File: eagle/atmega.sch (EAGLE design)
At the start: 40 parts, among them IC1 TO 5V, Q1 16MHz, U1 ATMEGA328P-AU

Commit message: Ładniej wygląda, dodałem transobtor zamiast fotorezystorów. Podłączenie komparatorów
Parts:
- removed FOTO1, FOTO2, FOTO3, FOTO4: (no value), pinhead:PINHD-1X3
- removed PH1, PH2, PH3, PH4: M9960_11B, photo-elements:M9960_11B
- added IC2: LM339D, linear:LM339D
- added JP1, JP2, JP3, JP4: (no value), pinhead:PINHD-1X3
- added R10, R14, R17: 100k, rcl:R-EU_R0805
- added R11: 220, rcl:R-EU_R0805
- added R12, R15, R18, R7, R8: 220R, rcl:R-EU_R0805
- added R13, R16, R9: 22k, rcl:R-EU_R0805
- added U$2, U$3, U$4, U$5: CNY70, cny70:CNY70
- LED1, LED3, LED4, LED5: device led:LED5MM -> led:LEDCHIPLED_0805
- R1: device resistor:R-EU_0204/7 -> rcl:R-EU_R0805
- R2: value (none) -> 220R; device resistor:R-EU_M0805 -> rcl:R-EU_R0805
- R3: value (none) -> 22k; device resistor:R-EU_0204/5 -> rcl:R-EU_R0805
- R4: value (none) -> 100k; device resistor:R-EU_0204/5 -> rcl:R-EU_R0805
- R5, R6: value (none) -> 220R; device resistor:R-EU_0204/5 -> rcl:R-EU_R0805
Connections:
- net N$2 renamed KWARC1
- net N$3 renamed KWARC2
- removed net N$33: FOTO4.3, U1.PC3
- removed net PC0: PH1.2, R3.1
- removed net PC1: PH2.2, R4.1
- removed net PC2: PH3.2, R5.1
- removed net PC3: PH4.2, R6.1
- new net KO1: IC2A.OUT, PROGRAMMER.1, R4.1, R6.1, U1.PB5
- new net KO2: IC2B.OUT, PROGRAMMER.2, R10.1, R12.1, U1.PB4
- new net KO3: IC2C.OUT, PROGRAMMER.3, R14.1, R15.1, U1.PB3
- new net KO4: IC2D.OUT, R17.1, R18.1, U1.PB2
- new net KOM1: IC2A.+IN, JP1.1, R3.1
- new net KOM2: IC2B.+IN, JP2.1, R9.1
- new net KOM3: IC2C.+IN, JP3.1, R13.1
- new net KOM4: IC2D.+IN, JP4.1, R16.1
- new net N$2: LED3.C, R12.2
- new net N$20: LED1.C, R6.2
- new net N$3: U$2.COL
- new net N$36: U$5.COL
- new net POT: IC2A.-IN, IC2B.-IN, IC2C.-IN, IC2D.-IN
- new net VZ: C4.2, C5.+, U$1.VM1, U$1.VM2, U$1.VM3
- net GND: now also JP1.3, JP2.3, JP3.3, JP4.3, R11.1, U$2.C, U$2.EMI, U$3.C, U$3.EMI, U$4.C, U$4.EMI, U$5.C, U$5.EMI; no longer LED1.C, LED3.C, LED4.C, LED5.C, R2.2, R3.2, R4.2, R5.2, R6.2
- net N$10: now also R5.1, U$4.A; no longer PROGRAMMER.1, U1.PB5
- net N$21: now also LED4.C, R15.2; no longer C4.2, C5.+
- net N$23: now also U$3.COL; no longer FOTO1.2, FOTO2.2, FOTO3.2, FOTO4.2
- net N$28: now also R7.1, U$3.A; no longer LED2.C, R2.1
- net N$29: now also LED5.C, R18.2; no longer FOTO1.3, U1.PC0
- net N$30: now also U$4.COL; no longer FOTO2.3, U1.PC1
- net N$32: now also R8.1, U$5.A; no longer FOTO3.3, U1.PC2
- net N$4: now also R1.2; no longer R1.1
- net N$5: now also R1.1; no longer R1.2
- net N$7: now also LED2.C, R11.2; no longer PROGRAMMER.2, U1.PB4
- net N$9: now also R2.1, U$2.A; no longer PROGRAMMER.3, U1.PB3
- net VCC: now also JP1.2, JP2.2, JP3.2, JP4.2, R10.2, R13.2, R14.2, R16.2, R17.2, R2.2, R3.2, R4.2, R5.2, R7.2, R8.2, R9.2; no longer FOTO1.1, FOTO2.1, FOTO3.1, FOTO4.1, PH1.1, PH2.1, PH3.1, PH4.1, U$1.VM1, U$1.VM2, U$1.VM3
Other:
- note added: "Czujnik podłaża lewy przedni"
- note added: "Czujnik podłaża lewy tylny"
- note added: "Czujnik podłaża prawy przedni"
- note added: "Czujnik podłaża prawy tylny"
- note added: "Filtrowanie do zasilania sterownika"
- note added: "Komparator do czujnika Lewy przedni"
- note added: "Komparator do czujnika Lewy tylny"
- note added: "Komparator do czujnika Prawy przedni"
- note added: "Komparator do czujnika Prawy tylny"
- note added: "Kwarc do Atmegi"
- note added: "To KOM1"
- note added: "To Kom 2"
- note added: "To Kom 3"
- note added: "To Kom 4"
- moved on the sheet: C1, C2, C4, C5, LED1, LED3, LED4, LED5, Q1, R1, R2, R3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

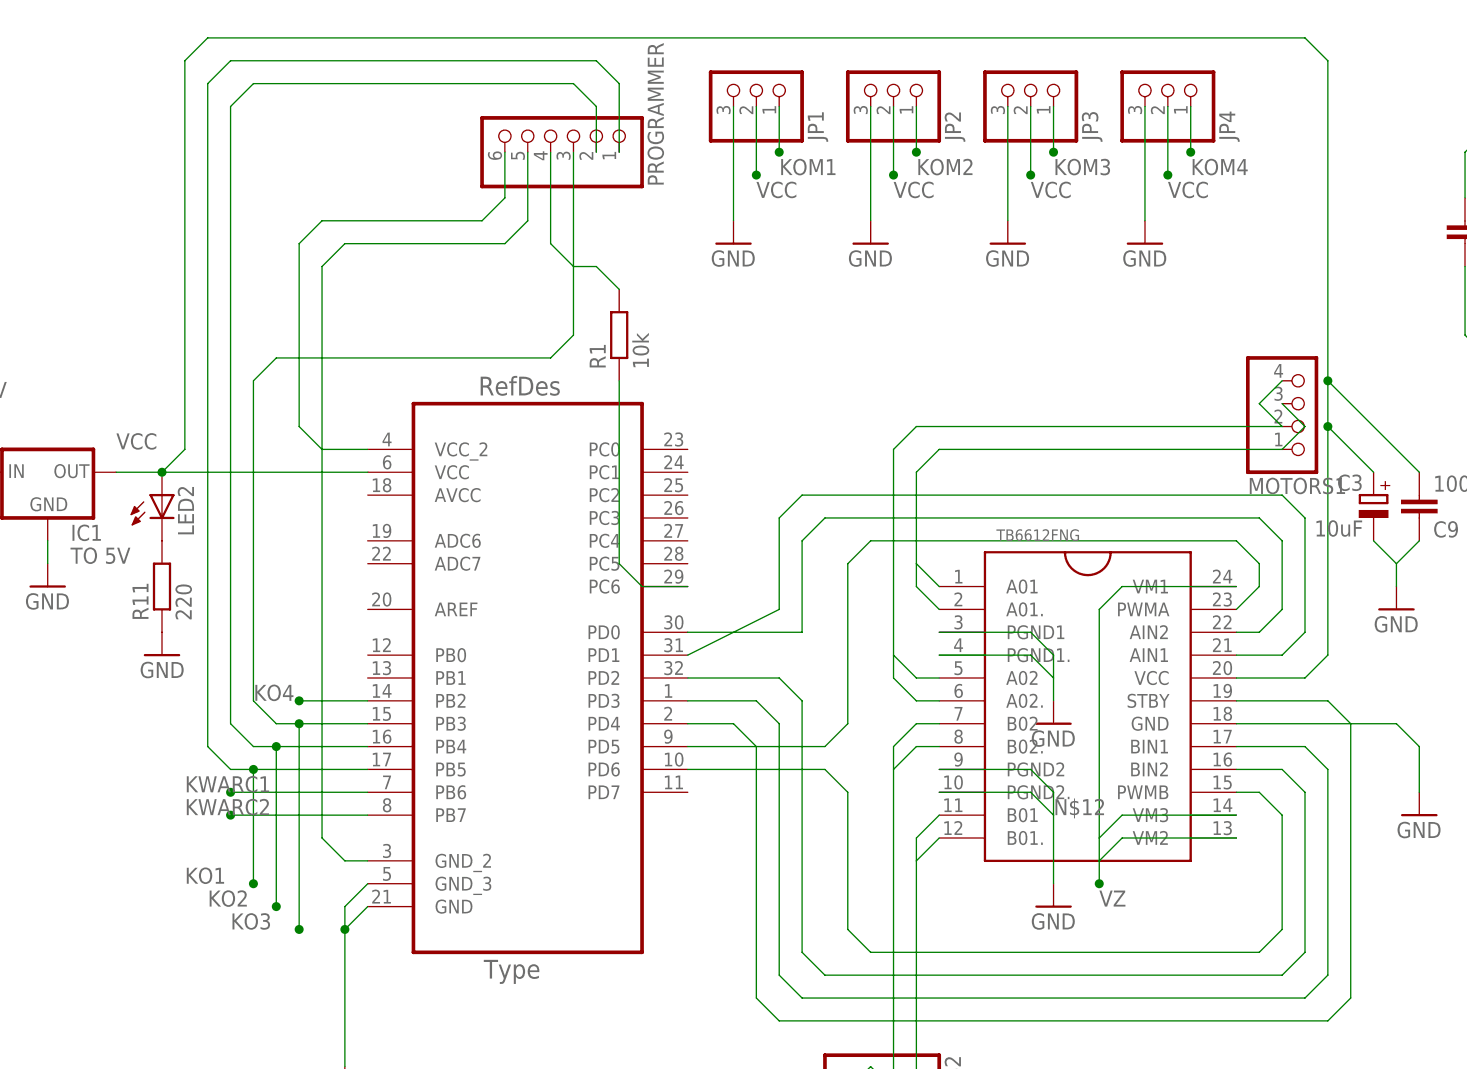
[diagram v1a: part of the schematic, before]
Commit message: zmiana pinów ICSP (programowanie) z 6x1 na 2x3
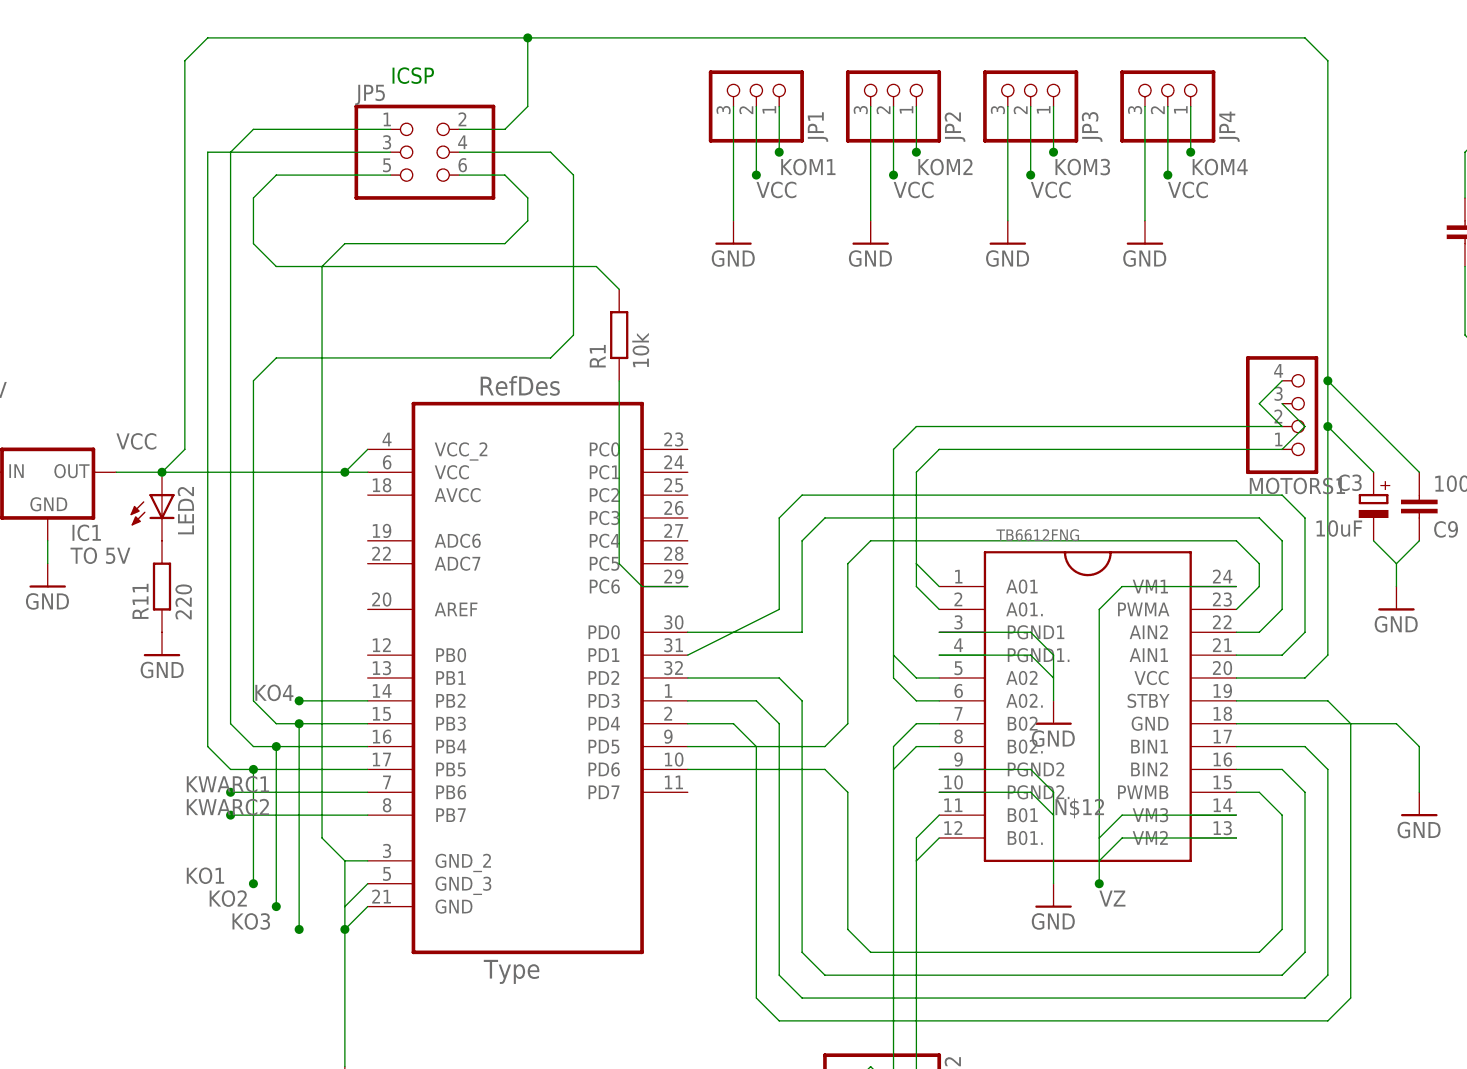
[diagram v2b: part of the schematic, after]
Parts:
- removed PROGRAMMER: (no value), pinhead:PINHD-1X6M
- added JP5: (no value), pinhead:PINHD-2X3
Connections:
- removed net N$11: PROGRAMMER.5, U1.GND_2
- removed net N$6: PROGRAMMER.6, U1.VCC_2
- net GND: now also JP5.6, U1.GND_2
- net KO1: now also JP5.3; no longer PROGRAMMER.1
- net KO2: now also JP5.1; no longer PROGRAMMER.2
- net KO3: now also JP5.4; no longer PROGRAMMER.3
- net N$4: now also JP5.5; no longer PROGRAMMER.4
- net VCC: now also JP5.2, U1.VCC_2
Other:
- note added: "ICSP"

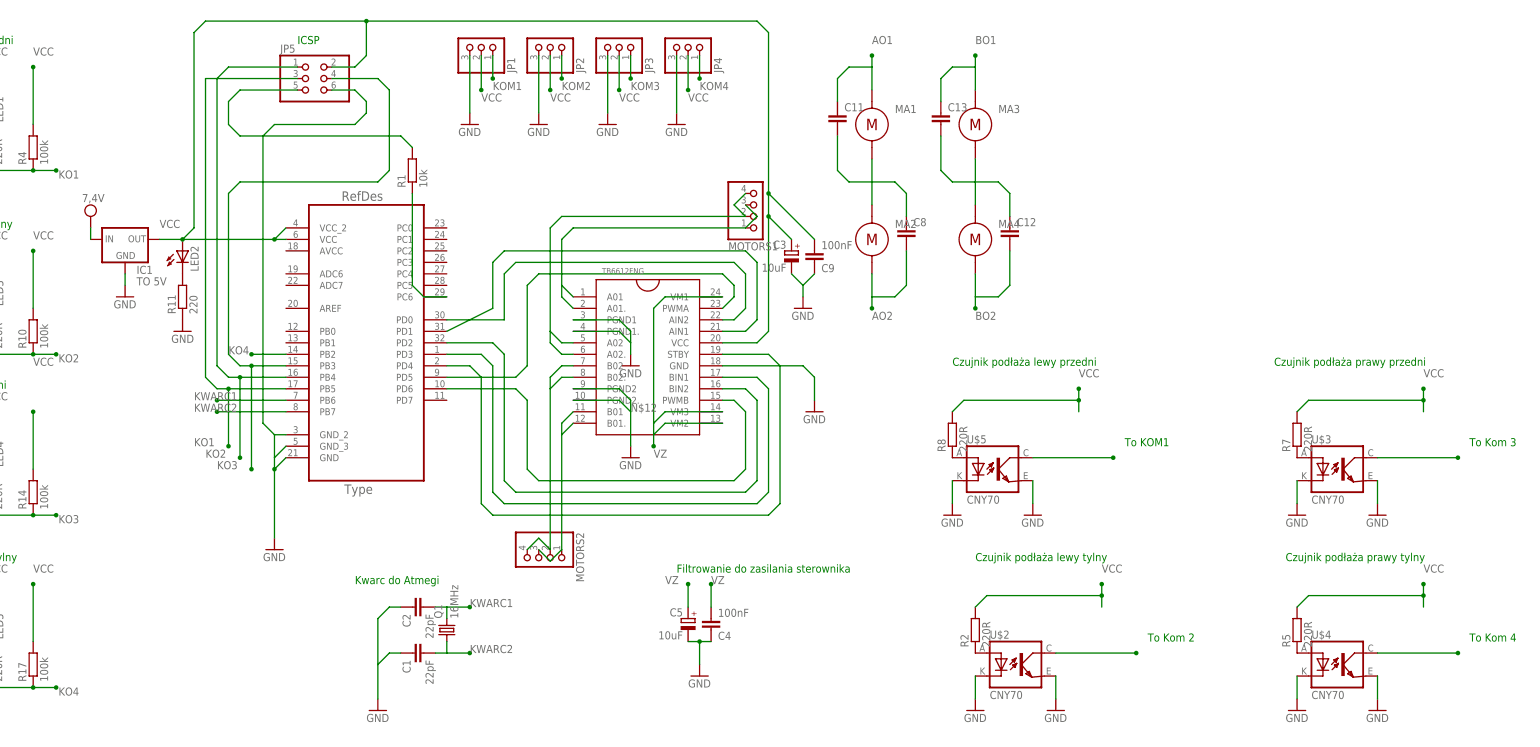
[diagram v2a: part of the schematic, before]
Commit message: zmiana pinów wychodzący (silniki) piny na czujniki, skończone podłączanie elementów.
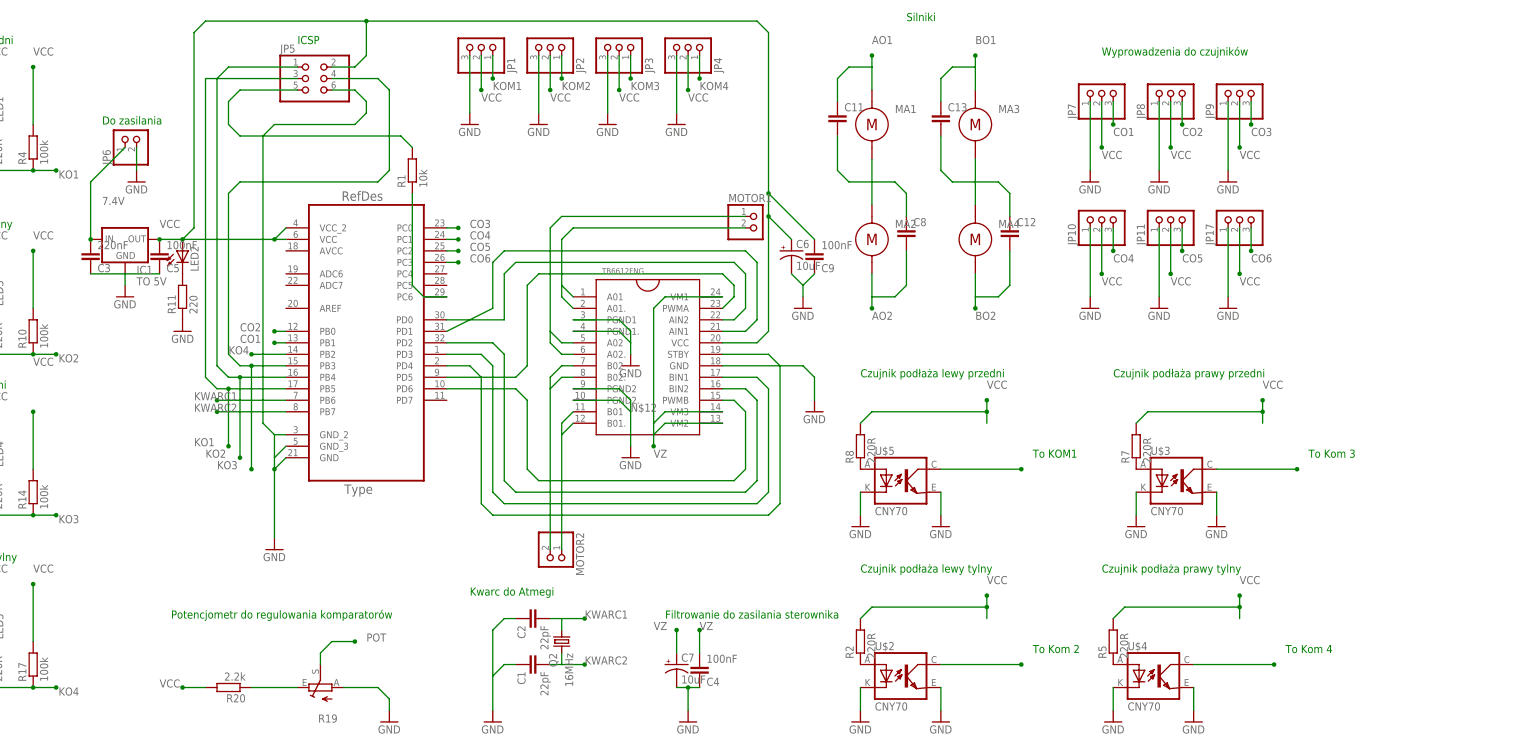
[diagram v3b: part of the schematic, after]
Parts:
- removed MOTORS1, MOTORS2: (no value), pinhead:PINHD-1X4
- removed Q1: 16MHz, crystal:CRYSTALHC49S
- added C6, C7: 10uF, SparkFun-Capacitors:22UF-POLAR-PANASONIC_C-35V-20%
- added JP10, JP11, JP17, JP7, JP8, JP9: (no value), pinhead:PINHD-1X3
- added JP6, MOTOR1, MOTOR2: (no value), pinhead:PINHD-1X2
- added Q2: 16MHz, crystal:CSM-7X-DU
- added R19: (no value), pot:TRIM_EU-B25P
- added R20: 2.2k, rcl:R-EU_R0805
- C3: value 10uF -> 220nF; device rcl:CPOL-EU140CLH-1010 -> capacitor-wima:C2,5-3; SPICEPREFIX (none) -> C
- C5: value 10uF -> 100nF; device rcl:CPOL-EU140CLH-1010 -> capacitor-wima:C2,5-3; SPICEPREFIX (none) -> C
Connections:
- net N$5 renamed CO9
- new net 7.4V: C3.2, IC1.IN, JP6.1
- new net CO1: JP7.3, U1.PB1
- new net CO2: JP8.3, U1.PB0
- new net CO3: JP9.3, U1.PC0
- new net CO4: JP10.3, U1.PC1
- new net CO5: JP11.3, U1.PC2
- new net CO6: JP17.3, U1.PC3
- new net N$6: R19.E, R20.1
- net GND: now also C3.1, C5.1, JP10.1, JP11.1, JP17.1, JP6.2, JP7.1, JP8.1, JP9.1, R19.A
- net KWARC1: now also Q2.1; no longer Q1.2
- net KWARC2: now also Q2.2; no longer Q1.1
- net N$19: now also MOTOR2.1; no longer MOTORS2.1, MOTORS2.3
- net N$22: now also MOTOR1.2; no longer MOTORS1.1, MOTORS1.3
- net N$24: now also MOTOR2.2; no longer MOTORS2.2, MOTORS2.4
- net N$27: now also MOTOR1.1; no longer MOTORS1.2, MOTORS1.4
- net N$31: now also C6.-, C7.-; no longer C3.-, C5.-
- net POT: now also R19.S
- net VCC: now also C5.2, C6.+, JP10.2, JP11.2, JP17.2, JP7.2, JP8.2, JP9.2, R20.2; no longer C3.+, IC1.IN
- net VZ: now also C7.+; no longer C5.+
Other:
- note added: "Do zasilania"
- note added: "Potencjometr do regulowania komparatorów"
- note added: "Silniki"
- note added: "Wyprowadzenia do czujników"
- moved on the sheet: C1, C2, C4, R2, R5, R7, R8, U$2, U$3, U$4, U$5

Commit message: Zmiany podłączenia. Rozpoczęgie pracy nad płyką PCB.
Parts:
- removed R1: 10k, rcl:R-EU_R0805
- added R21: 10k, rcl:R-EU_R0805
- added ZWORKA: (no value), rcl:R-EU_0613/5V
- renumbered JP1 to FOTO1, JP10 to OD4, JP11 to OD5, JP17 to OD6, JP2 to FOTO2, JP3 to FOTO3, JP4 to FOTO4, JP5 to ICSP, JP6 to VOLTAGE, JP7 to OD1, JP8 to OD2, JP9 to OD3
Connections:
- net N$18 renamed PWMA
- net N$19 renamed OUTMB1
- net N$22 renamed OUTMA1
- net N$24 renamed OUTMB2
- net N$27 renamed OUTMA2
- removed net CO9: R1.1, U1.PC6
- removed net N$1: U$1.AIN1, U1.PD1
- removed net N$12: U$1.PGND2, U$1.PGND2.
- removed net N$13: U$1.BIN1, U1.PD3
- removed net N$14: U$1.STBY
- removed net N$15: U$1.BIN2, U1.PD2
- removed net N$16: U$1.PWMB, U1.PD6
- removed net N$17: U1.PD4
- removed net N$25: U$1.AIN2, U1.PD0
- removed net N$4: ICSP.5, R1.2
- new net AIN1: U$1.AIN1, U1.PD7
- new net AIN2: U$1.AIN2, U1.PD6
- new net BIN1: U$1.BIN1, U1.PB1
- new net BIN2: U$1.BIN2, U1.PB2
- new net PROG: ICSP.1, U1.PB4
- new net PWMB: ICSP.4, U$1.PWMB, U1.PB3
- new net RESET: ICSP.5, R21.2
- new net RESET1: U1.PC6, ZWORKA.1
- new net RESET3: R21.1, ZWORKA.2
- new net STBY: U$1.STBY, U1.PB0
- net CO1: now also ICSP.3, U1.PB5; no longer U1.PB1
- net CO2: now also U1.PC0; no longer U1.PB0
- net CO3: now also U1.PC1; no longer U1.PC0
- net CO4: now also U1.PC2; no longer U1.PC1
- net CO5: now also U1.PC3; no longer U1.PC2
- net CO6: now also U1.PD0; no longer U1.PC3
- net GND: now also C4.1, C7.-, U$1.PGND2, U$1.PGND2.; no longer U1.GND, U1.GND_2
- net KO1: now also U1.PD4; no longer ICSP.3, U1.PB5
- net KO2: now also U1.PD3; no longer ICSP.1, U1.PB4
- net KO3: now also U1.PD1; no longer ICSP.4, U1.PB3
- net KO4: now also U1.PD2; no longer U1.PB2
- net N$31: no longer C4.1, C7.-
- net VCC: no longer U1.VCC
- net VZ: no longer U$1.VM1
